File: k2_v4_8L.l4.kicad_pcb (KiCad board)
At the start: 8 copper layers, 120 x 46 mm, 42 parts, among them J11 J_EC_HEADER, J12 J_12V_IN, J13 J_SWD, J2 SlimSAS_x8_SFF8654, J3 MCIO_4i_SFF1016, J4 MCIO_4i_SFF1016, J6 J_PWR_CTRL, J9 J_OOB_HEADER, U1 STM32G0B1CBT6, U2 DCDC_12V_3V3, U4 BAT54C, U5 OPTO_LTV356T, U6 DS320PR1601

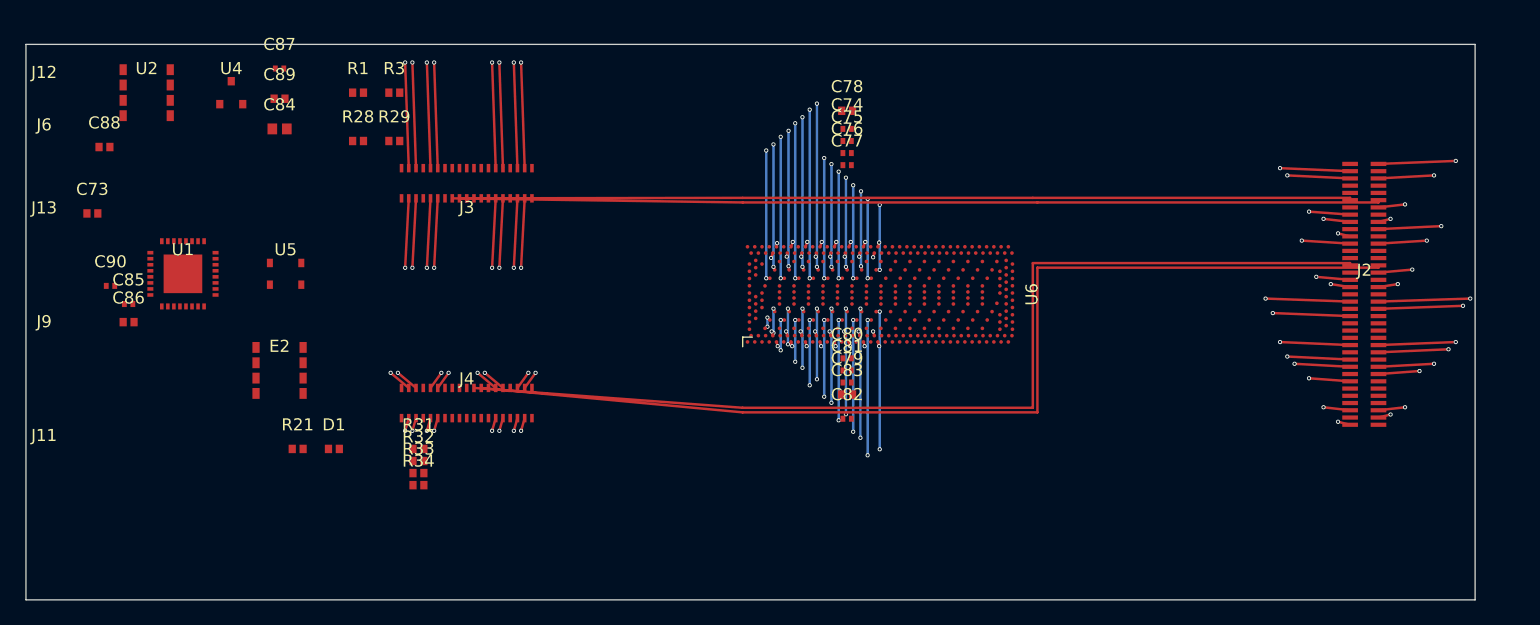
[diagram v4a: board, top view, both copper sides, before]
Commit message: CO-23: 板边真带落地（Edge.Cuts 33.0/79.0）— D1 copper_edge 12->0、D2 hole_to_hole 3->0；DFM new 88->73
引擎 W3-CN.37（canonical 37d2d05db8418526 FEASIBLE_ALL，skew 0.0031）；分配工件 CO16-ALLOC.4 e5d30cd4eac83e16
（西 WLO 33.70/WSTEP 1.05 带下压 + WSWAP 1-11(UP2<->DN7) + J2STEP 0.58 + COLMODE=pol + HOLE_GAP 0.4495；东 EDELTA -0.10）。
G4/G5/G6 PASS；G7 SI PASS / DFM FAIL(new 73，全为既有 PCIE_REFCLK0/1 族，D3 独立变更单)。

独立复核（续接会话 ARCHER-2）：引擎/分配/W4 逐字节复现；L4 validator L4-A..E viol=0；
独立 kicad-cli DRC 复算 HEAD new 88 -> CO-23 new 73（copper_edge 0 / hole_to_hole 0）；SI skew 0.0031；四冻结源未变。
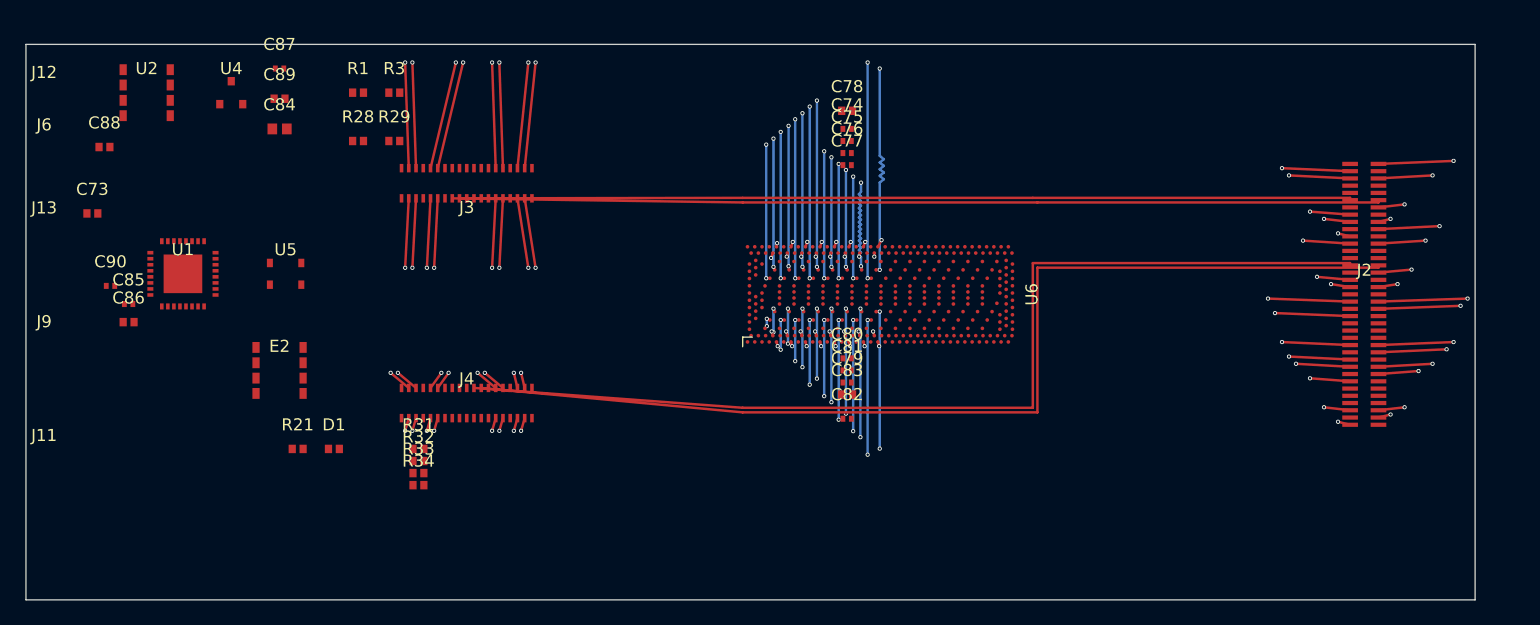
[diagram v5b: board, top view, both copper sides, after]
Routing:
- net PCIE_DN_OUT7_N_MCIO: track 50.9 -> 74.5 mm
- net PCIE_DN_OUT7_P_MCIO: track 50.9 -> 74.5 mm
- net PCIE_UP2_P: track 55.5 -> 53.4 mm
- net PCIE_UP2_N: track 55.5 -> 53.4 mm
- net PCIE_UP6_N: track 49.0 -> 51.1 mm
- net PCIE_UP6_P: track 49.0 -> 51.1 mm
- net PCIE_UP5_N: track 54.9 -> 56.8 mm
- net PCIE_UP5_P: track 54.9 -> 56.8 mm
- net PCIE_UP4_N: track 57.7 -> 59.5 mm
- net PCIE_UP4_P: track 57.7 -> 59.5 mm
- net PCIE_UP7_N: track 46.7 -> 48.4 mm
- net PCIE_UP7_P: track 46.7 -> 48.4 mm
- net PCIE_DN_OUT6_P_MCIO: track 56.6 -> 58.0 mm
- net PCIE_DN_OUT6_N_MCIO: track 56.6 -> 58.0 mm
- net PCIE_DN_OUT5_N_MCIO: track 60.2 -> 61.5 mm
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
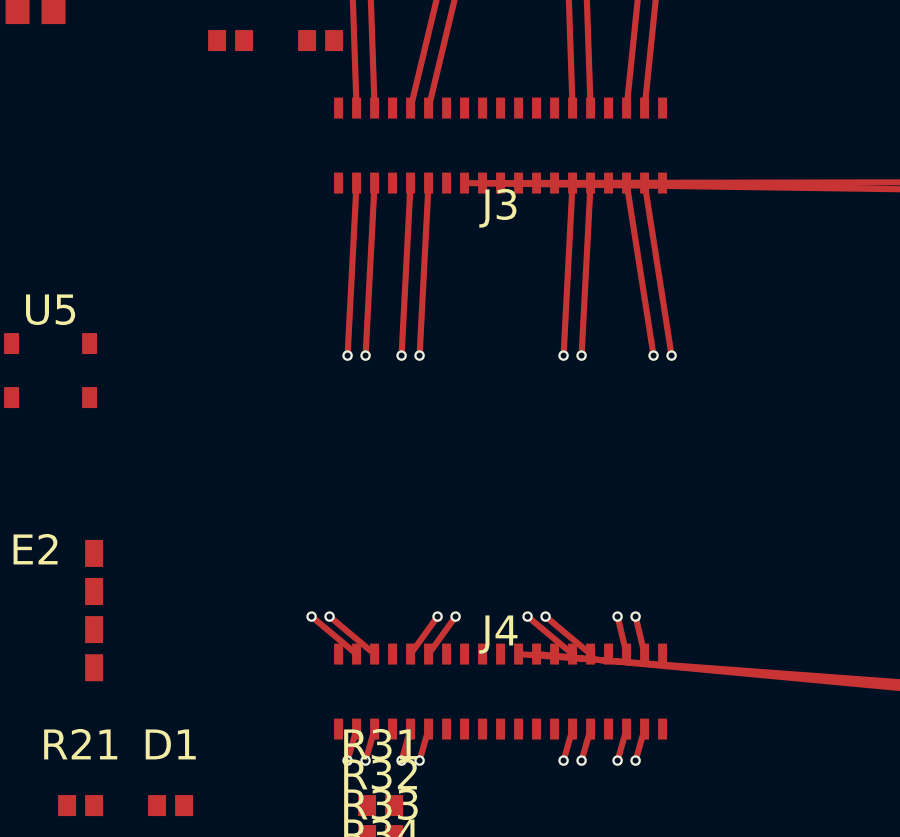
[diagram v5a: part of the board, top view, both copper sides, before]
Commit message: CO-36: D3b 收官 — connector 落列器按 land 段长升序（CO10_LXPRIO=landlen）；ALLOC.5 0bf6cdc203887a48 + W3-CN.38 0261e0b0a598df6d；32/32 且 pad 铜距 shop-clean（CO-25 6 条全消）；G4/G5/G6 PASS、DFM new 73->65；LID.1 层意图与 L1 pad/球分配未动
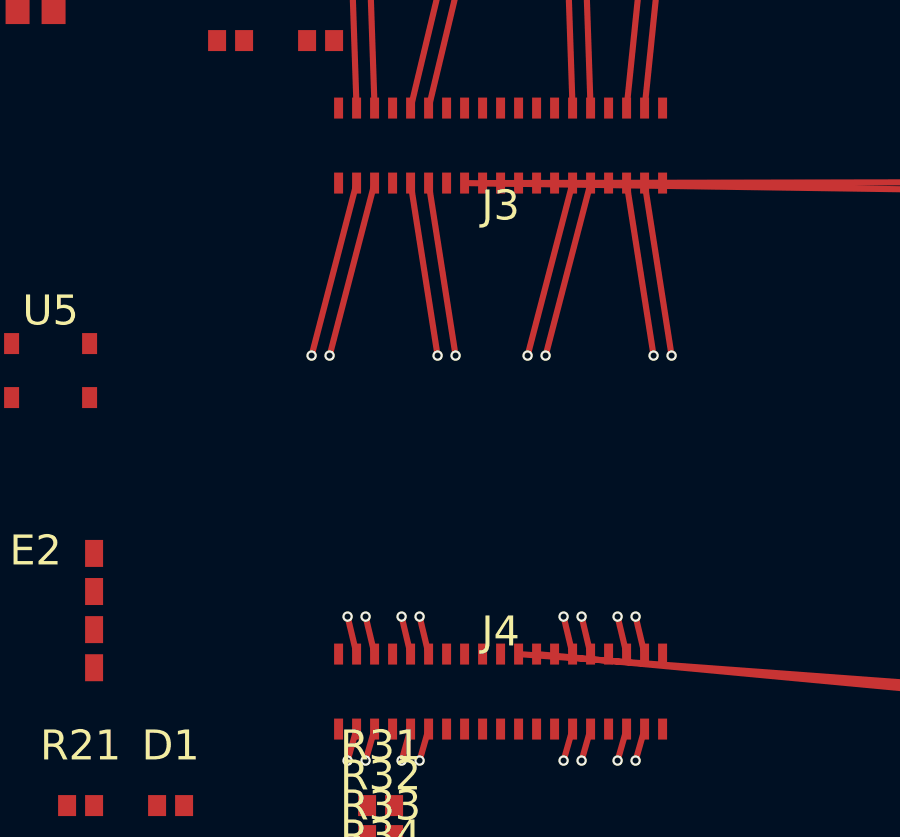
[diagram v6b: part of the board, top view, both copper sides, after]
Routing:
- net PCIE_DN_OUT6_P_MCIO: track 58.0 -> 56.2 mm
- net PCIE_DN_OUT6_N_MCIO: track 58.0 -> 56.2 mm
- net PCIE_DN_OUT4_P_MCIO: track 67.0 -> 65.2 mm
- net PCIE_DN_OUT4_N_MCIO: track 67.0 -> 65.2 mm
- net PCIE_DN_OUT3_P_MCIO: track 67.8 -> 69.1 mm
- net PCIE_DN_OUT3_N_MCIO: track 67.8 -> 69.1 mm
- net PCIE_DN_OUT1_N_MCIO: track 54.0 -> 55.4 mm
- net PCIE_DN_OUT1_P_MCIO: track 54.0 -> 55.4 mm
- net PCIE_DN_OUT2_N_MCIO: track 62.7 -> 61.5 mm
- net PCIE_DN_OUT2_P_MCIO: track 62.7 -> 61.5 mm
- net PCIE_DN_OUT5_P_MCIO: track 61.5 -> 62.5 mm
- net PCIE_DN_OUT5_N_MCIO: track 61.5 -> 62.5 mm

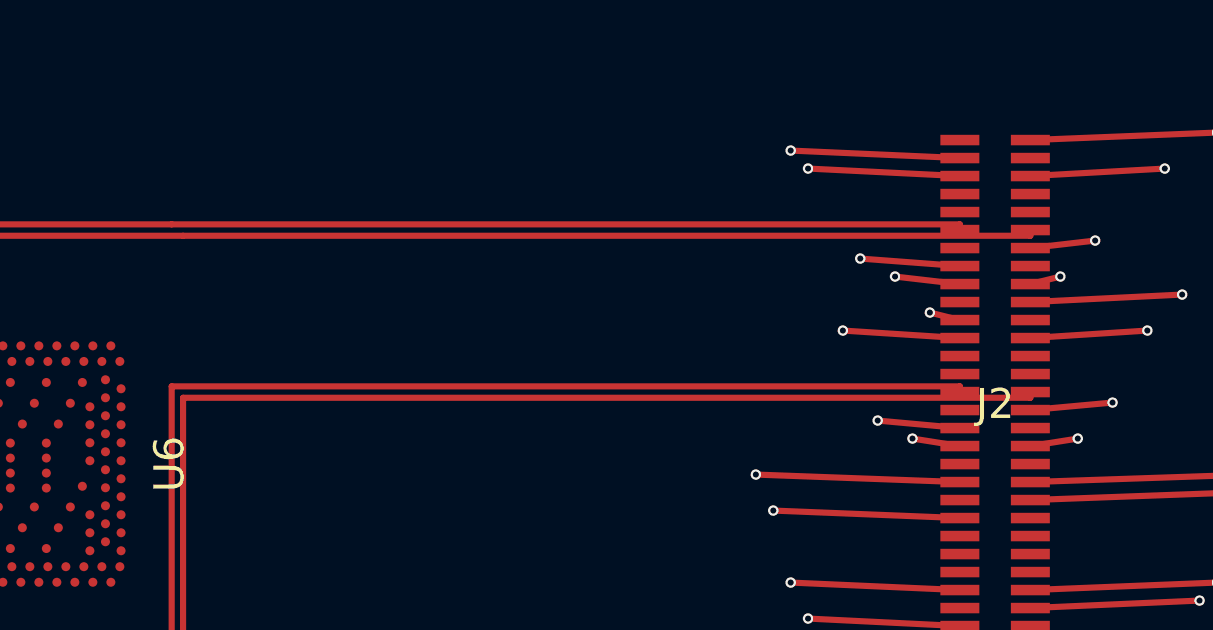
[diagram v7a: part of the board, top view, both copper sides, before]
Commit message: CO-41: ECS-001 落地（REFCLK J2 侧 F.Cu->In2->F.Cu 单次换层）— 引擎 W3-CN.39 发射 3D nodes（FEASIBLE_ALL/crossings 0/A-CN.1..9 PASS）+ L4 与验证器消费 nodes（L4-A..E viol 0；segs 2408->2413、vias 248->252=每 N 线 +2 via）+ spec 指针->rev-3；DFM new 60->54（shorting 9->5、mask 38->36）；实测残余 54 中仅 2 条在 J2 pad 场、52 条在远端（REFCLK 轨沿 J3/J4 A 排平行穿越 -> mask 36 + short/crossing/clearance）=> CO-38「J2 全责」不成立，主因=远端接入窗口（witness v2 未覆盖）；已在册回退记录：N 轨偏移 0.19->0.31 会撞 C80 元件体 keepout（A-CN.5a FAIL）
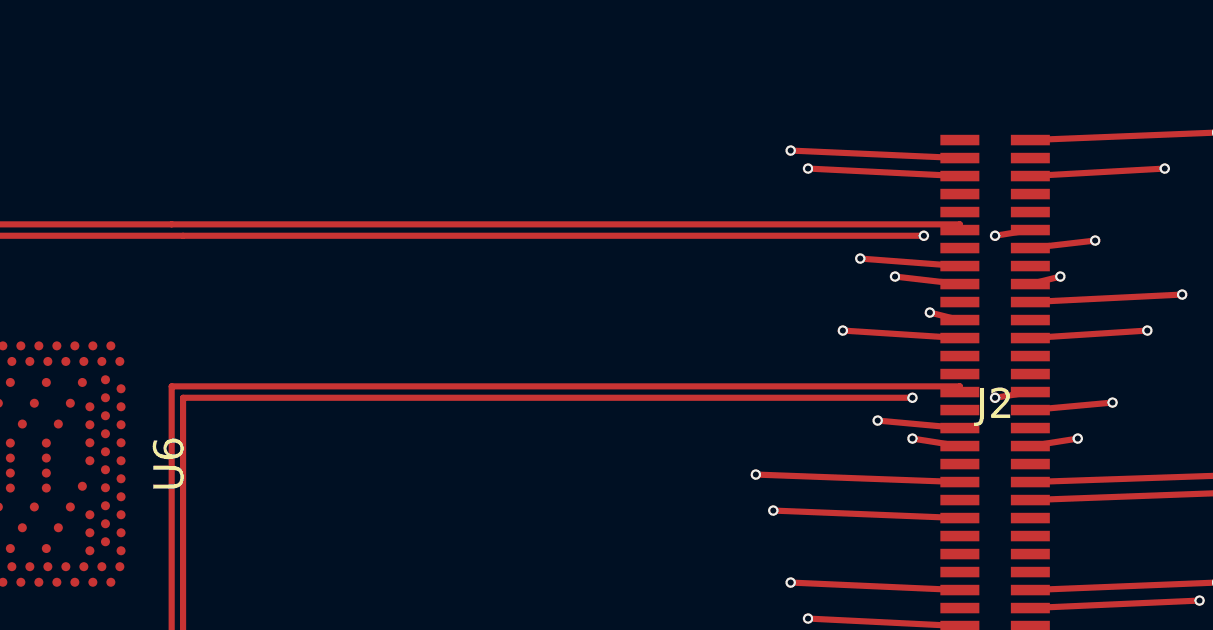
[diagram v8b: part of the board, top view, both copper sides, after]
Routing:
- net PCIE_REFCLK1_N: track 86.6 -> 93.1 mm, vias 0 -> 2
- net PCIE_REFCLK0_N: track 76.9 -> 76.7 mm, vias 0 -> 2
